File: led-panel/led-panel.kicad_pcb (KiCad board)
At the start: 2 copper layers, 129 parts, among them J1 Conn_01x24

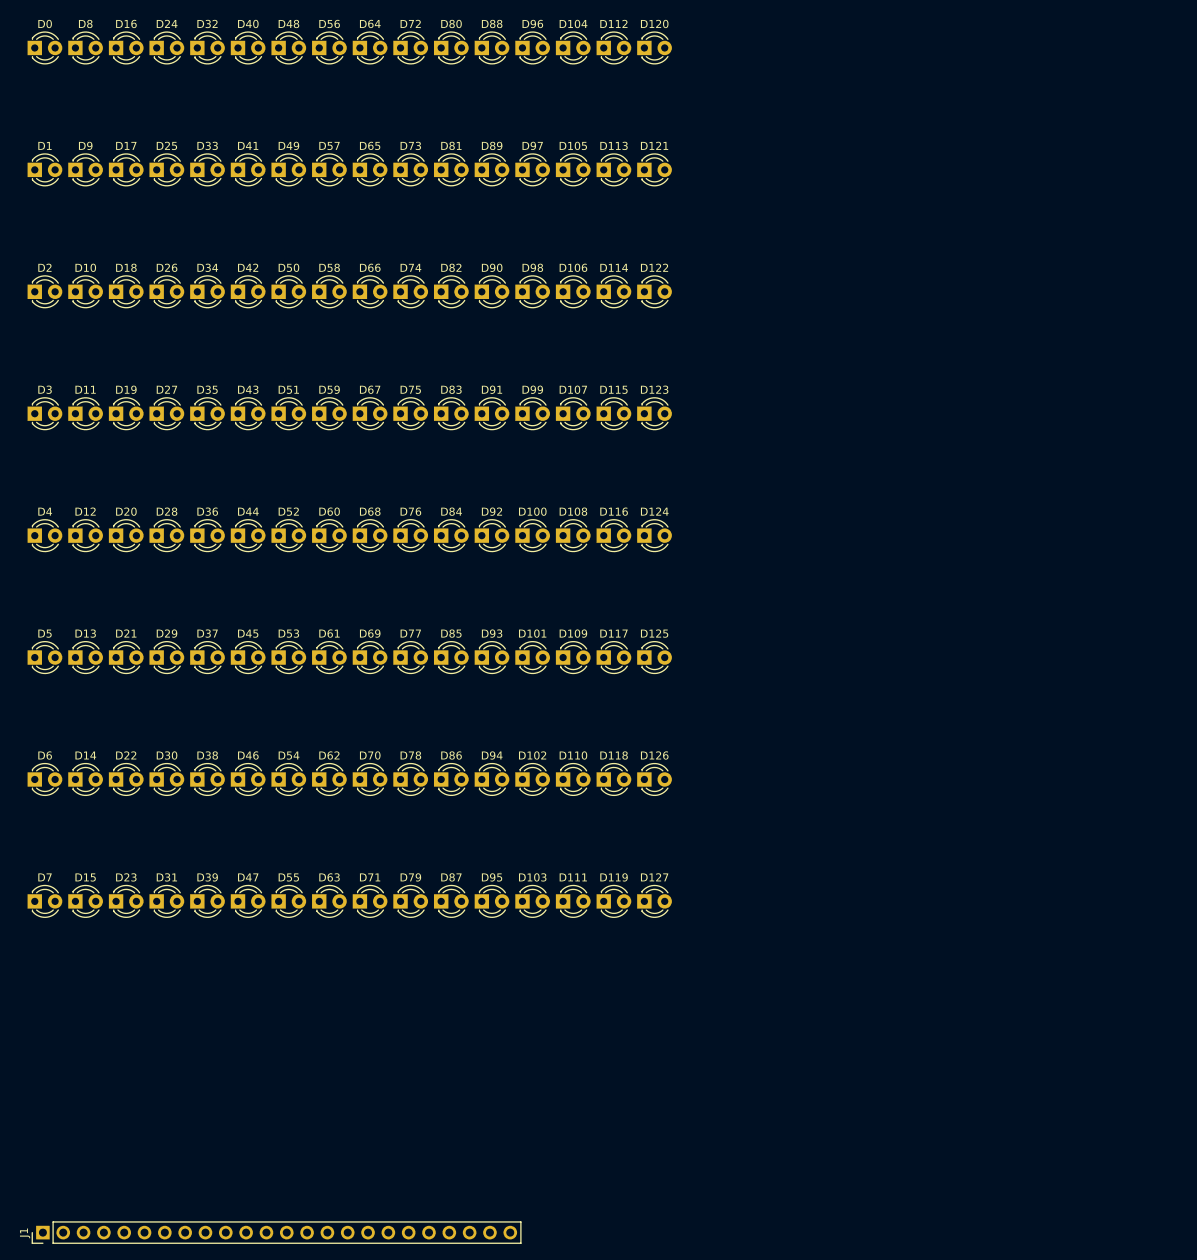
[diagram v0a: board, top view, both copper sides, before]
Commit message: components arranged
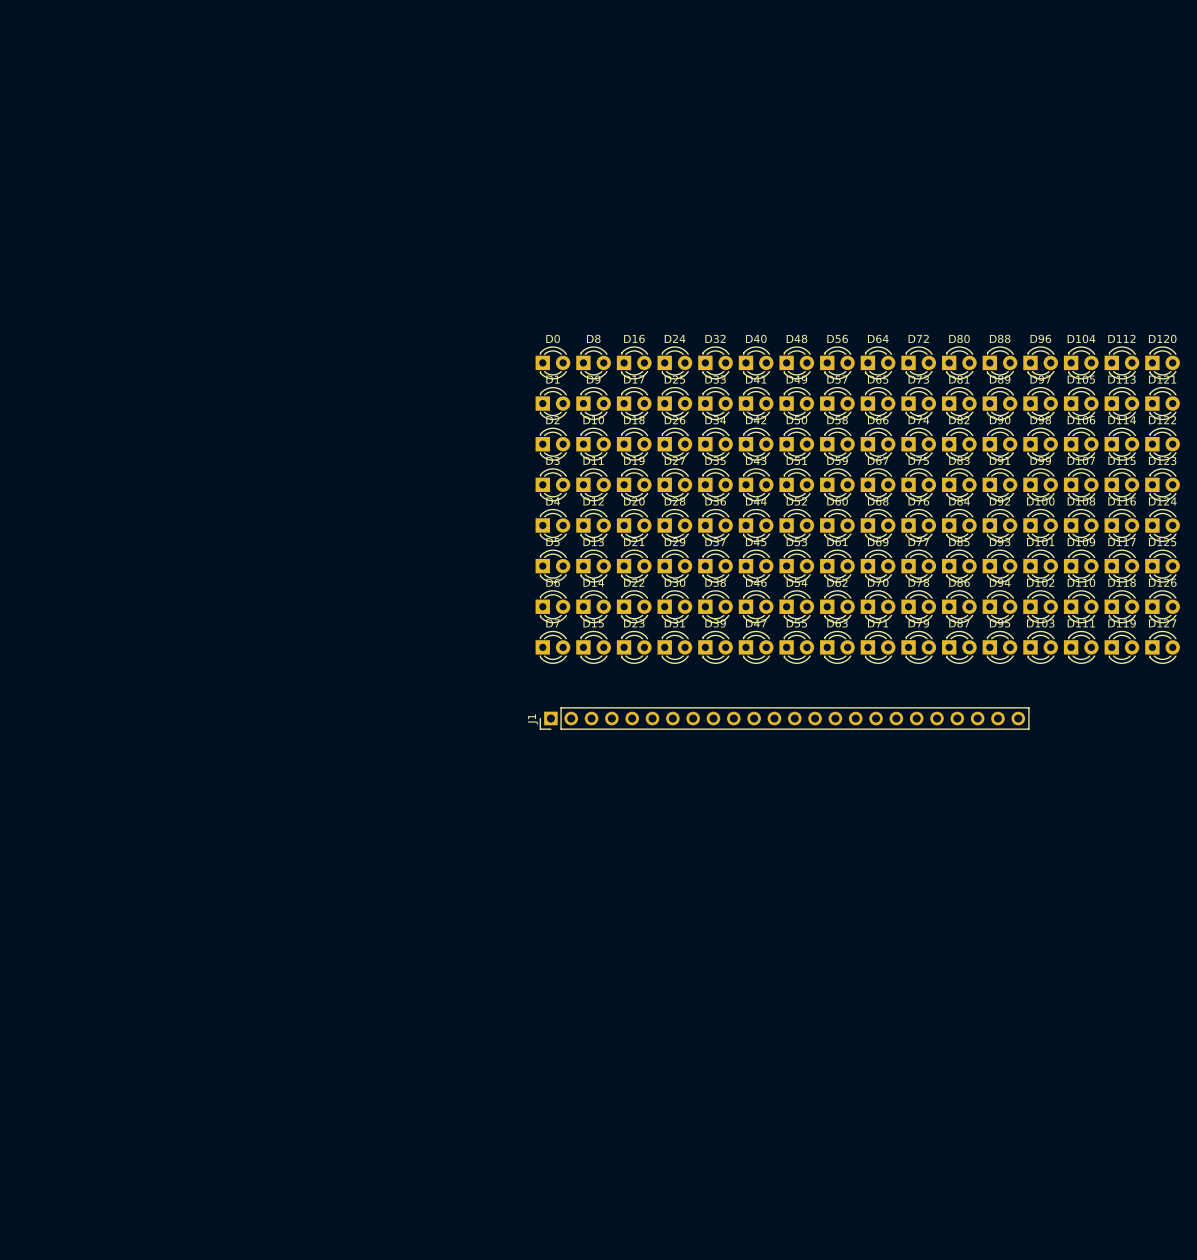
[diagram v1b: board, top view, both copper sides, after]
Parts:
- moved J1 90.3 mm to (109.0, 109.2)
- moved D0 74.7 mm to (108.0, 64.8)
- moved D104 74.7 mm to (174.0, 64.8)
- moved D112 74.7 mm to (179.1, 64.8)
- moved D120 74.7 mm to (184.2, 64.8)
- moved D16 74.7 mm to (118.1, 64.8)
- moved D24 74.7 mm to (123.2, 64.8)
- moved D32 74.7 mm to (128.3, 64.8)
- moved D40 74.7 mm to (133.3, 64.8)
- moved D48 74.7 mm to (138.4, 64.8)
- moved D64 74.7 mm to (148.6, 64.8)
- moved D8 74.7 mm to (113.0, 64.8)
- moved D80 74.7 mm to (158.8, 64.8)
- moved D88 74.7 mm to (163.8, 64.8)
- moved D96 74.7 mm to (168.9, 64.8)
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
